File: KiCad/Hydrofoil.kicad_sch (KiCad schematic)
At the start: 19 parts, among them J1 Conn_01x05_Pin, U1 LM334M, U2 LM334M, U3 ADS1115IDGS

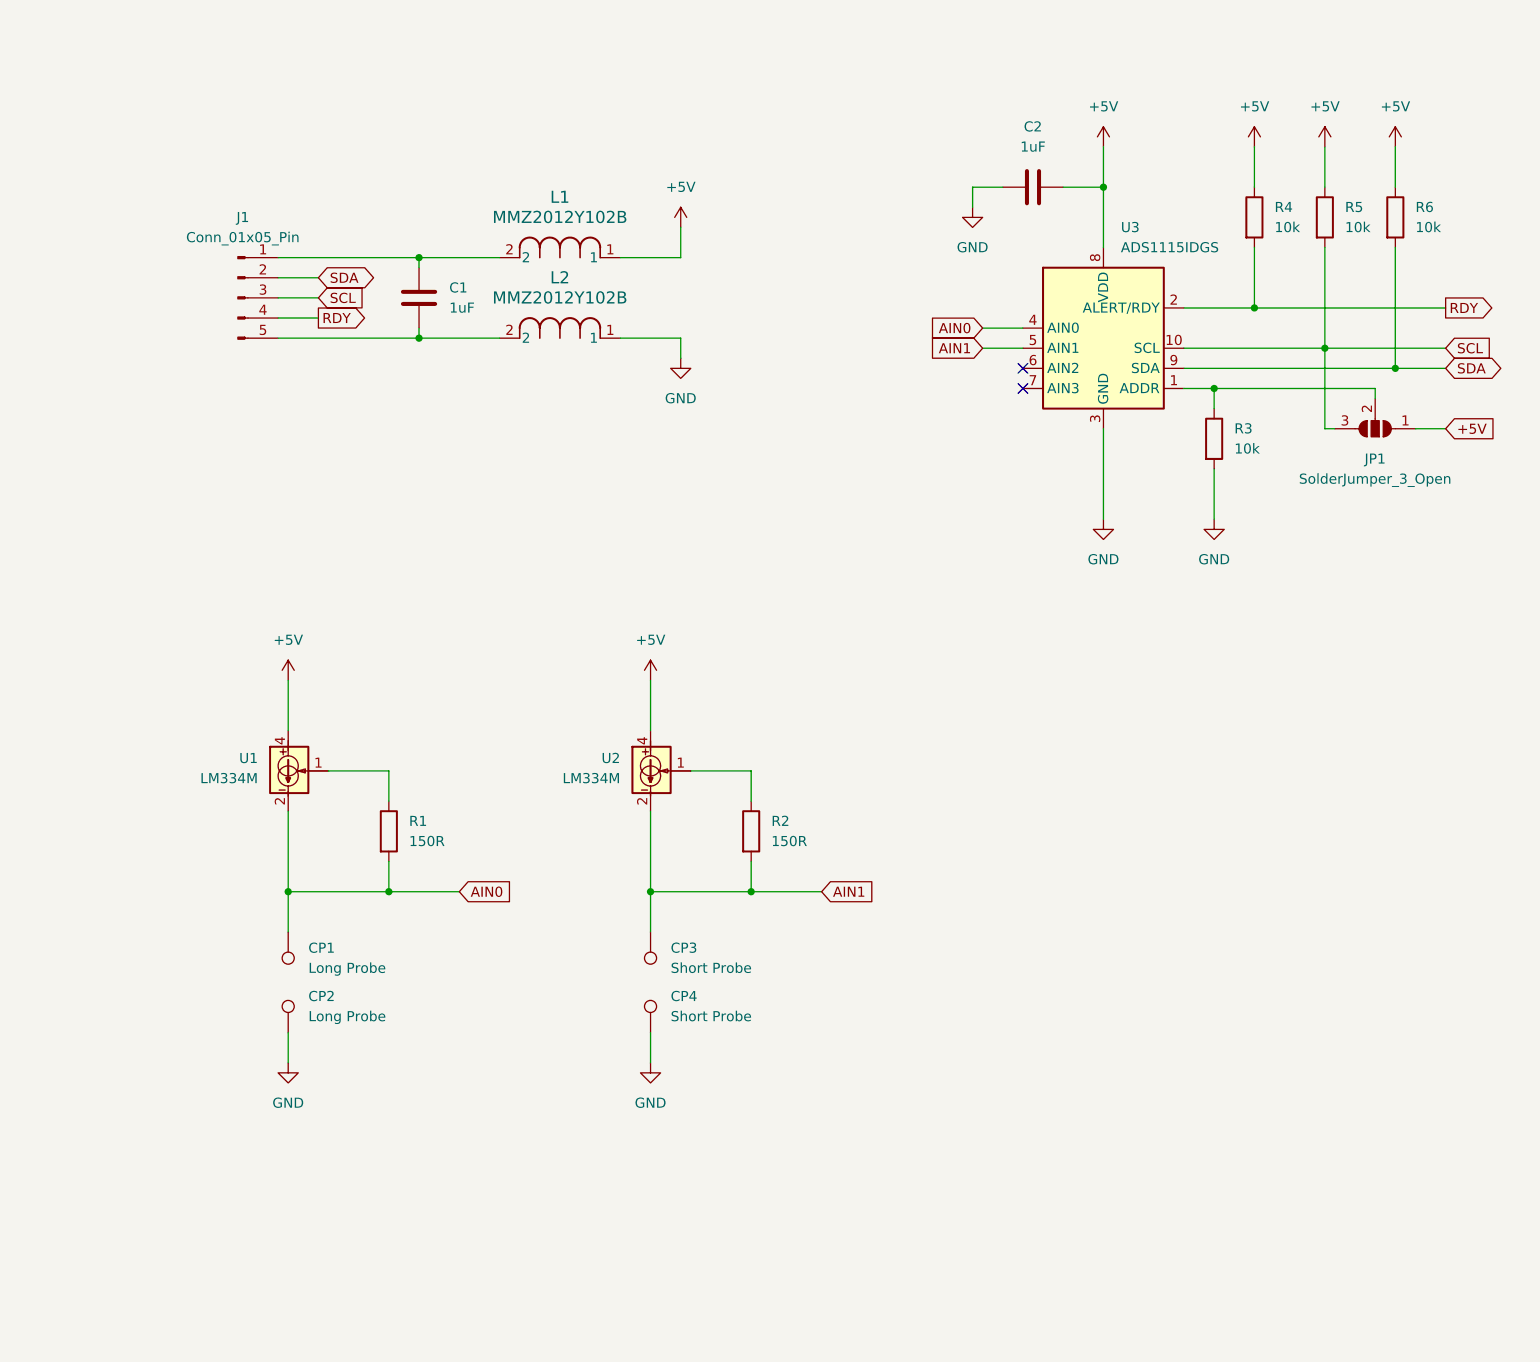
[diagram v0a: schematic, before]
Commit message: Finalize edgecut, device arrangement, wiring
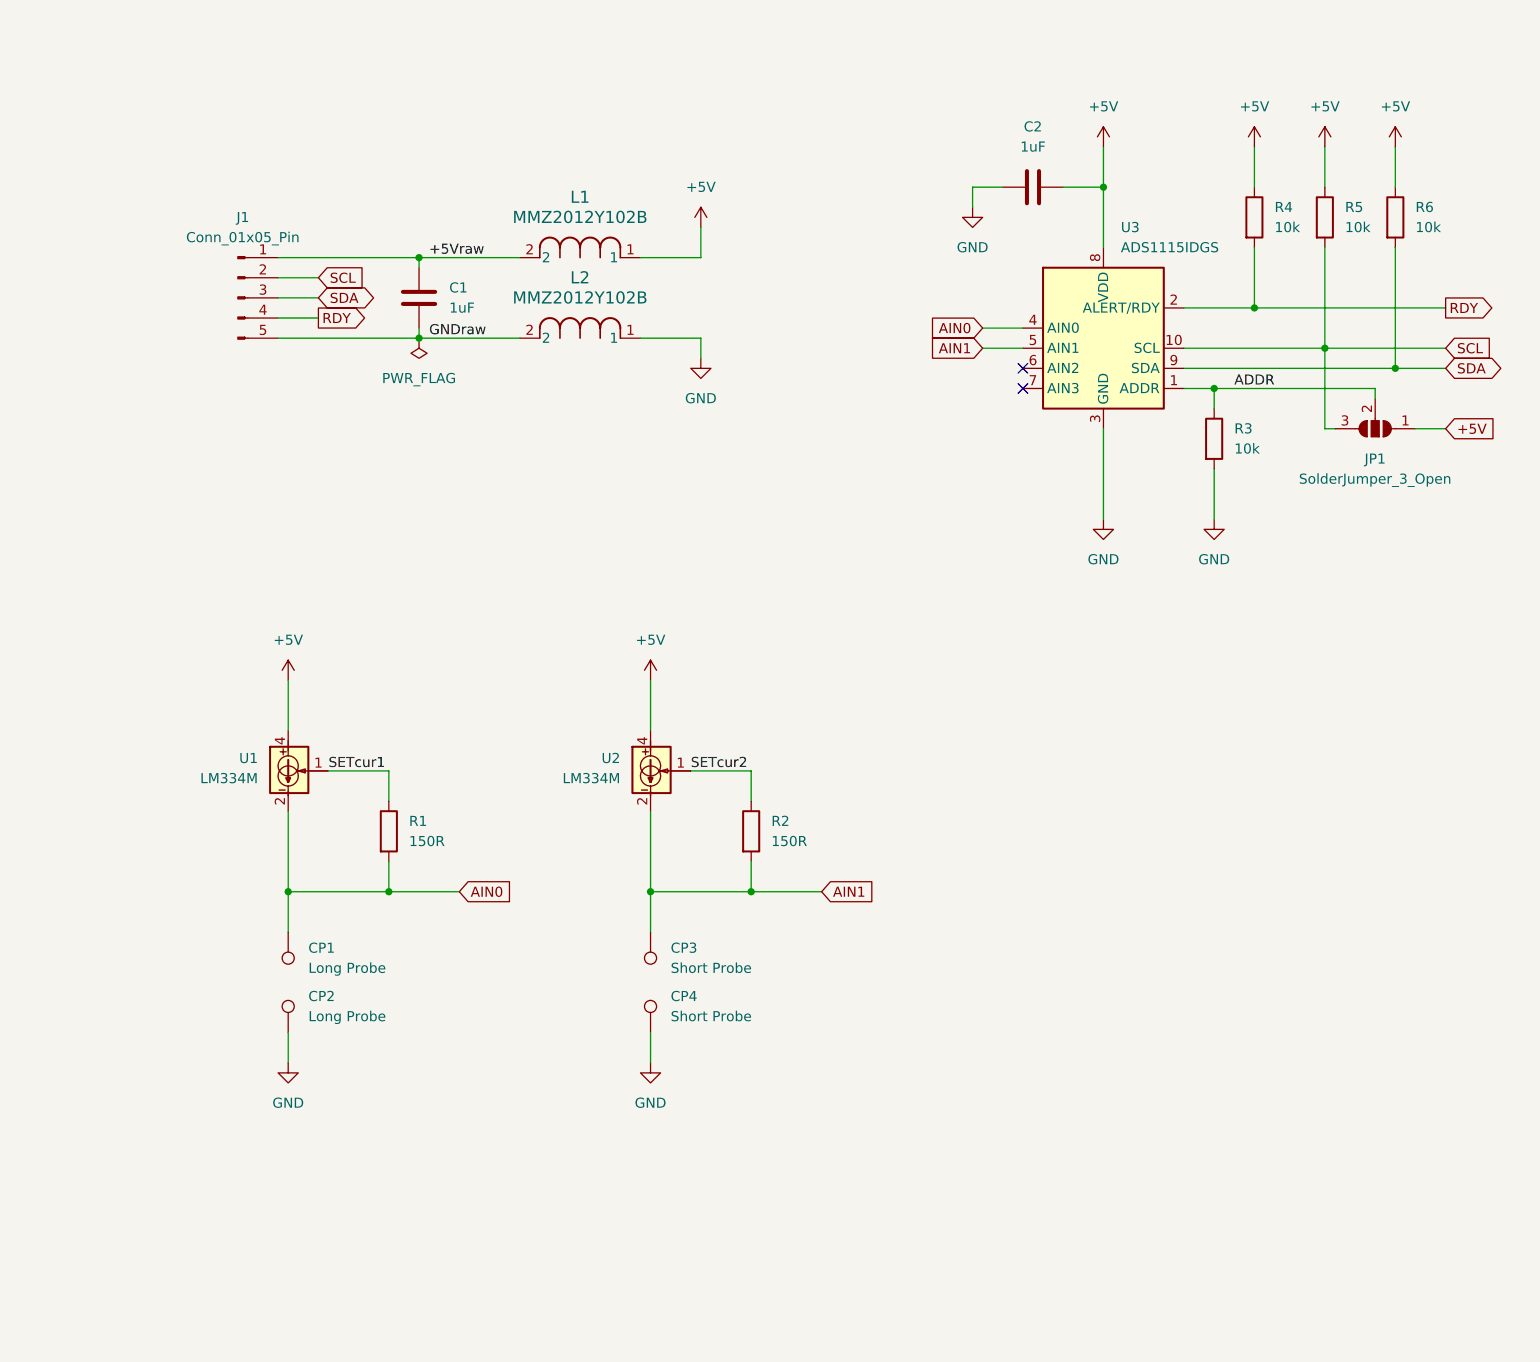
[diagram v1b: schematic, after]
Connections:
- net SCL: now also J1.2 (Pin_2); no longer J1.3 (Pin_3)
- net SDA: now also J1.3 (Pin_3); no longer J1.2 (Pin_2)
- net SETcur2: now reaches R2.1, U2.1
- net ADDR: now reaches JP1.2 (C), R3.1, U3.1 (ADDR)
- net +5Vraw: now reaches C1.1, J1.1 (Pin_1), L1.2
- net GNDraw: now reaches C1.2, J1.5 (Pin_5), L2.2
- net SETcur1: now reaches R1.1, U1.1
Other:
- moved on the sheet: L1, L2
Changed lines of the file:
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@@
     (stroke (width 0) (type default))
   )
-  (wire (pts (xy 109.22 50.8) (xy 109.22 54.61))
+  (wire (pts (xy 111.76 50.8) (xy 111.76 54.61))
     (stroke (width 0) (type default))
   )
@@
     (stroke (width 0) (type default))
   )
-  (wire (pts (xy 76.2 54.61) (xy 58.42 54.61))
-    (stroke (width 0) (type default))
-  )
   (wire (pts (xy 190.5 76.2) (xy 191.77 76.2))
     (stroke (width 0) (type default))
@@
     (stroke (width 0) (type default))
   )
+  (wire (pts (xy 58.42 59.69) (xy 63.5 59.69))
+    (stroke (width 0) (type default))
+  )
   (wire (pts (xy 190.5 76.2) (xy 190.5 66.04))
     (stroke (width 0) (type default))
   )
-  (wire (pts (xy 101.6 64.77) (xy 109.22 64.77))
+  (wire (pts (xy 104.14 64.77) (xy 111.76 64.77))
     (stroke (width 0) (type default))
   )
@@
     (stroke (width 0) (type default))
   )
+  (wire (pts (xy 58.42 57.15) (xy 63.5 57.15))
+    (stroke (width 0) (type default))
+  )
   (wire (pts (xy 201.93 76.2) (xy 205.74 76.2))
     (stroke (width 0) (type default))
@@
     (stroke (width 0) (type default))
   )
+  (wire (pts (xy 58.42 54.61) (xy 76.2 54.61))
+    (stroke (width 0) (type default))
+  )
   (wire (pts (xy 76.2 54.61) (xy 76.2 55.88))
     (stroke (width 0) (type default))
@@
     (stroke (width 0) (type default))
   )
-  (wire (pts (xy 76.2 64.77) (xy 86.36 64.77))
+  (wire (pts (xy 76.2 64.77) (xy 88.9 64.77))
     (stroke (width 0) (type default))
   )
@@
     (stroke (width 0) (type default))
   )
-  (wire (pts (xy 58.42 59.69) (xy 63.5 59.69))
-    (stroke (width 0) (type default))
-  )
   (wire (pts (xy 105.41 152.4) (xy 105.41 156.21))
     (stroke (width 0) (type default))
@@
     (stroke (width 0) (type default))
   )
-  (wire (pts (xy 86.36 54.61) (xy 76.2 54.61))
+  (wire (pts (xy 76.2 54.61) (xy 88.9 54.61))
     (stroke (width 0) (type default))
   )
@@
     (stroke (width 0) (type default))
   )
-  (wire (pts (xy 58.42 57.15) (xy 63.5 57.15))
-    (stroke (width 0) (type default))
-  )
-  (wire (pts (xy 109.22 54.61) (xy 101.6 54.61))
-    (stroke (width 0) (type default))
-  )
-  (wire (pts (xy 109.22 67.31) (xy 109.22 64.77))
-    (stroke (width 0) (type default))
+  (wire (pts (xy 111.76 54.61) (xy 104.14 54.61))
+    (stroke (width 0) (type default))
+  )
+  (wire (pts (xy 111.76 67.31) (xy 111.76 64.77))
+    (stroke (width 0) (type default))
+  )
+  (label "GNDraw" (at 77.47 64.77 0) (fields_autoplaced)
+    (effects (font (size 1.27 1.27)) (justify left bottom))
+    (property "Netclass" "GND" (at 77.47 66.04 0)
+      (effects (font (size 1.27 1.27) italic) (justify left))
+    )
+  )
+  (label "+5Vraw" (at 77.47 54.61 0) (fields_autoplaced)
+    (effects (font (size 1.27 1.27)) (justify left bottom))
+    (property "Netclass" "5V" (at 77.47 55.88 0)
+      (effects (font (size 1.27 1.27) italic) (justify left))
+    )
+  )
+  (label "SETcur2" (at 110.49 119.38 0) (fields_autoplaced)
+    (effects (font (size 1.27 1.27)) (justify left bottom))
+    (property "Netclass" "Default" (at 110.49 120.65 0)
+      (effects (font (size 1.27 1.27) italic) (justify left))
+    )
+  )
+  (label "ADDR" (at 179.07 71.12 0) (fields_autoplaced)
+    (effects (font (size 1.27 1.27)) (justify left bottom))
+    (property "Netclass" "Default" (at 179.07 72.39 0)
+      (effects (font (size 1.27 1.27) italic) (justify left))
+    )
+  )
+  (label "SETcur1" (at 64.77 119.38 0) (fields_autoplaced)
+    (effects (font (size 1.27 1.27)) (justify left bottom))
+    (property "Netclass" "Default" (at 64.77 120.65 0)
+      (effects (font (size 1.27 1.27) italic) (justify left))
+    )
   )
   (global_label "SDA" (shape bidirectional) (at 205.74 68.58 0) (fields_autoplaced)
@@
     )
   )
-  (global_label "SDA" (shape bidirectional) (at 63.5 57.15 0) (fields_autoplaced)
+  (global_label "SDA" (shape bidirectional) (at 63.5 59.69 0) (fields_autoplaced)
     (effects (font (size 1.27 1.27)) (justify left))
-    (property "Intersheetrefs" "${INTERSHEET_REFS}" (at 71.1646 57.15 0)
+    (property "Intersheetrefs" "${INTERSHEET_REFS}" (at 71.1646 59.69 0)
       (effects (font (size 1.27 1.27)) (justify left) hide)
     )
@@
     )
   )
-  (global_label "SCL" (shape input) (at 63.5 59.69 0) (fields_autoplaced)
+  (global_label "SCL" (shape input) (at 63.5 57.15 0) (fields_autoplaced)
     (effects (font (size 1.27 1.27)) (justify left))
-    (property "Intersheetrefs" "${INTERSHEET_REFS}" (at 69.9928 59.69 0)
+    (property "Intersheetrefs" "${INTERSHEET_REFS}" (at 69.9928 57.15 0)
       (effects (font (size 1.27 1.27)) (justify left) hide)
     )
@@
     )
   )
+  (symbol (lib_id "power:PWR_FLAG") (at 76.2 64.77 180) (unit 1)
+    (in_bom yes) (on_board yes) (dnp no) (fields_autoplaced)
+    (property "Reference" "#FLG01" (at 76.2 66.675 0)
+      (effects (font (size 1.27 1.27)) hide)
+    )
+    (property "Value" "PWR_FLAG" (at 76.2 69.85 0)
+      (effects (font (size 1.27 1.27)))
+    )
+    (property "Footprint" "" (at 76.2 64.77 0)
+      (effects (font (size 1.27 1.27)) hide)
+    )
+    (property "Datasheet" "~" (at 76.2 64.77 0)
+      (effects (font (size 1.27 1.27)) hide)
+    )
+    (pin "1")
+    (instances
+      (project "Hydrofoil"
+        (path "/00ecf259-f619-4dbe-851b-92d463e0b367"
+          (reference "#FLG01") (unit 1)
+        )
+      )
+    )
+  )
   (symbol (lib_id "power:+5V") (at 162.56 40.64 0) (unit 1)
     (in_bom yes) (on_board yes) (dnp no)
@@
     )
   )
-  (symbol (lib_id "2023-09-04_18-15-31:MMZ2012Y102B") (at 86.36 54.61 0) (unit 1)
-    (in_bom yes) (on_board yes) (dnp no) (fields_autoplaced)
-    (property "Reference" "L1" (at 93.98 46.99 0)
+  (symbol (lib_id "2023-09-04_18-15-31:MMZ2012Y102B") (at 88.9 54.61 0) (unit 1)
+    (in_bom yes) (on_board yes) (dnp no) (fields_autoplaced)
+    (property "Reference" "L1" (at 96.52 46.99 0)
       (effects (font (size 1.524 1.524)))
     )
-    (property "Value" "MMZ2012Y102B" (at 93.98 49.53 0)
+    (property "Value" "MMZ2012Y102B" (at 96.52 49.53 0)
       (effects (font (size 1.524 1.524)))
     )
-    (property "Footprint" "Inductor_SMD:L_0805_2012Metric_Pad1.05x1.20mm_HandSolder" (at 86.36 54.61 0)
+    (property "Footprint" "Inductor_SMD:L_0805_2012Metric_Pad1.05x1.20mm_HandSolder" (at 88.9 54.61 0)
       (effects (font (size 1.27 1.27) italic) hide)
     )
-    (property "Datasheet" "MMZ2012Y102B" (at 86.36 54.61 0)
+    (property "Datasheet" "MMZ2012Y102B" (at 88.9 54.61 0)
       (effects (font (size 1.27 1.27) italic) hide)
     )
@@
     )
   )
-  (symbol (lib_id "power:GND") (at 109.22 67.31 0) (unit 1)
-    (in_bom yes) (on_board yes) (dnp no) (fields_autoplaced)
-    (property "Reference" "#PWR06" (at 109.22 73.66 0)
-      (effects (font (size 1.27 1.27)) hide)
-    )
-    (property "Value" "GND" (at 109.22 72.39 0)
-      (effects (font (size 1.27 1.27)))
-    )
-    (property "Footprint" "" (at 109.22 67.31 0)
-      (effects (font (size 1.27 1.27)) hide)
-    )
-    (property "Datasheet" "" (at 109.22 67.31 0)
+  (symbol (lib_id "power:GND") (at 111.76 67.31 0) (unit 1)
+    (in_bom yes) (on_board yes) (dnp no) (fields_autoplaced)
+    (property "Reference" "#PWR06" (at 111.76 73.66 0)
+      (effects (font (size 1.27 1.27)) hide)
+    )
+    (property "Value" "GND" (at 111.76 72.39 0)
+      (effects (font (size 1.27 1.27)))
+    )
+    (property "Footprint" "" (at 111.76 67.31 0)
+      (effects (font (size 1.27 1.27)) hide)
+    )
+    (property "Datasheet" "" (at 111.76 67.31 0)
       (effects (font (size 1.27 1.27)) hide)
     )
@@
     )
   )
-  (symbol (lib_id "power:+5V") (at 109.22 50.8 0) (unit 1)
-    (in_bom yes) (on_board yes) (dnp no) (fields_autoplaced)
-    (property "Reference" "#PWR05" (at 109.22 54.61 0)
-      (effects (font (size 1.27 1.27)) hide)
-    )
-    (property "Value" "+5V" (at 109.22 45.72 0)
-      (effects (font (size 1.27 1.27)))
-    )
-    (property "Footprint" "" (at 109.22 50.8 0)
-      (effects (font (size 1.27 1.27)) hide)
-    )
-    (property "Datasheet" "" (at 109.22 50.8 0)
+  (symbol (lib_id "power:+5V") (at 111.76 50.8 0) (unit 1)
+    (in_bom yes) (on_board yes) (dnp no) (fields_autoplaced)
+    (property "Reference" "#PWR05" (at 111.76 54.61 0)
+      (effects (font (size 1.27 1.27)) hide)
+    )
+    (property "Value" "+5V" (at 111.76 45.72 0)
+      (effects (font (size 1.27 1.27)))
+    )
+    (property "Footprint" "" (at 111.76 50.8 0)
+      (effects (font (size 1.27 1.27)) hide)
+    )
+    (property "Datasheet" "" (at 111.76 50.8 0)
       (effects (font (size 1.27 1.27)) hide)
     )
@@
     )
   )
-  (symbol (lib_id "2023-09-04_18-15-31:MMZ2012Y102B") (at 86.36 64.77 0) (unit 1)
-    (in_bom yes) (on_board yes) (dnp no) (fields_autoplaced)
-    (property "Reference" "L2" (at 93.98 57.15 0)
+  (symbol (lib_id "2023-09-04_18-15-31:MMZ2012Y102B") (at 88.9 64.77 0) (unit 1)
+    (in_bom yes) (on_board yes) (dnp no) (fields_autoplaced)
+    (property "Reference" "L2" (at 96.52 57.15 0)
       (effects (font (size 1.524 1.524)))
     )
-    (property "Value" "MMZ2012Y102B" (at 93.98 59.69 0)
+    (property "Value" "MMZ2012Y102B" (at 96.52 59.69 0)
       (effects (font (size 1.524 1.524)))
     )
-    (property "Footprint" "Inductor_SMD:L_0805_2012Metric_Pad1.05x1.20mm_HandSolder" (at 86.36 64.77 0)
+    (property "Footprint" "Inductor_SMD:L_0805_2012Metric_Pad1.05x1.20mm_HandSolder" (at 88.9 64.77 0)
       (effects (font (size 1.27 1.27) italic) hide)
     )
-    (property "Datasheet" "MMZ2012Y102B" (at 86.36 64.77 0)
+    (property "Datasheet" "MMZ2012Y102B" (at 88.9 64.77 0)
       (effects (font (size 1.27 1.27) italic) hide)
     )
